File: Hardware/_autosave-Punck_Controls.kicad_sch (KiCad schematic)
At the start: 36 parts, among them J1 Conn_01x12_Female, J10 Kick_In, J11 USB_B_Micro, J12 Tempo_Out, J13 Audio_Out_L, J14 Audio_Out_R, J15 Midi_In, J2 Conn_01x12_Female, J3 Conn_01x12_Female, J4 Conn_01x12_Female, J5 Snare_In, J6 CH_In, J7 OH_In, J8 SamplerA_In, J9 SamplerB_In

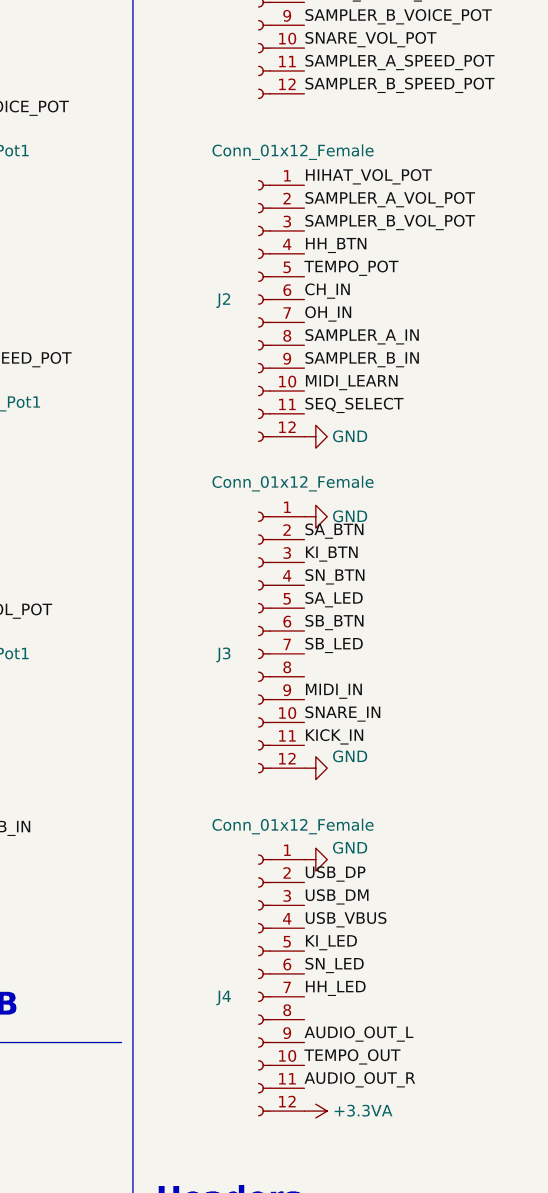
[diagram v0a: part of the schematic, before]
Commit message: Updated PCBs to match changes in panel; ground returns improved
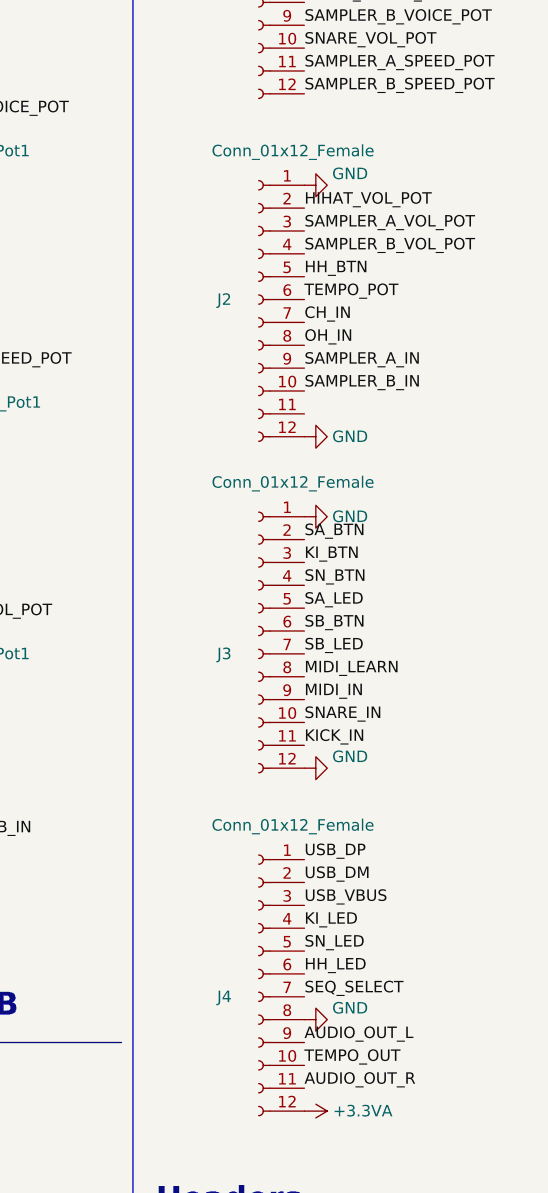
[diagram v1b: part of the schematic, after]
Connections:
- net CH_IN: now also J2.7 (Pin_7); no longer J2.6 (Pin_6)
- net GND: now also J2.1 (Pin_1), J4.8 (Pin_8); no longer J4.1 (Pin_1)
- net HH_BTN: now also J2.5 (Pin_5); no longer J2.4 (Pin_4)
- net HH_LED: now also J4.6 (Pin_6); no longer J4.7 (Pin_7)
- net HIHAT_VOL_POT: now also J2.2 (Pin_2); no longer J2.1 (Pin_1)
- net KI_LED: now also J4.4 (Pin_4); no longer J4.5 (Pin_5)
- net MIDI_LEARN: now also J3.8 (Pin_8); no longer J2.10 (Pin_10)
- net OH_IN: now also J2.8 (Pin_8); no longer J2.7 (Pin_7)
- net SAMPLER_A_IN: now also J2.9 (Pin_9); no longer J2.8 (Pin_8)
- net SAMPLER_A_VOL_POT: now also J2.3 (Pin_3); no longer J2.2 (Pin_2)
- net SAMPLER_B_IN: now also J2.10 (Pin_10); no longer J2.9 (Pin_9)
- net SAMPLER_B_VOL_POT: now also J2.4 (Pin_4); no longer J2.3 (Pin_3)
- net SEQ_SELECT: now also J4.7 (Pin_7); no longer J2.11 (Pin_11)
- net SN_LED: now also J4.5 (Pin_5); no longer J4.6 (Pin_6)
- net TEMPO_POT: now also J2.6 (Pin_6); no longer J2.5 (Pin_5)
- net USB_DM: now also J4.2 (Pin_2); no longer J4.3 (Pin_3)
- net USB_DP: now also J4.1 (Pin_1); no longer J4.2 (Pin_2)
- net USB_VBUS: now also J4.3 (Pin_3); no longer J4.4 (Pin_4)
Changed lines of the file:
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@@
     (effects (font (size 1.27 1.27)) (justify left bottom))
   )
-  (label "CH_IN" (at 252.73 71.12 0)
+  (label "CH_IN" (at 252.73 73.66 0)
     (effects (font (size 1.27 1.27)) (justify left bottom))
   )
@@
     (effects (font (size 1.27 1.27)) (justify left bottom))
   )
-  (label "KI_LED" (at 252.73 143.51 0)
-    (effects (font (size 1.27 1.27)) (justify left bottom))
-  )
-  (label "SAMPLER_A_VOL_POT" (at 252.73 60.96 0)
+  (label "KI_LED" (at 252.73 140.97 0)
+    (effects (font (size 1.27 1.27)) (justify left bottom))
+  )
+  (label "SAMPLER_A_VOL_POT" (at 252.73 63.5 0)
     (effects (font (size 1.27 1.27)) (justify left bottom))
   )
@@
     (effects (font (size 1.27 1.27)) (justify left bottom))
   )
-  (label "USB_DM" (at 252.73 138.43 0)
+  (label "USB_DM" (at 252.73 135.89 0)
     (effects (font (size 1.27 1.27)) (justify left bottom))
   )
@@
     (effects (font (size 1.27 1.27)) (justify left bottom))
   )
-  (label "USB_VBUS" (at 252.73 140.97 0)
+  (label "USB_VBUS" (at 252.73 138.43 0)
     (effects (font (size 1.27 1.27)) (justify left bottom))
   )
@@
     (effects (font (size 1.27 1.27)) (justify left bottom))
   )
-  (label "SEQ_SELECT" (at 252.73 83.82 0)
+  (label "SEQ_SELECT" (at 252.73 148.59 0)
     (effects (font (size 1.27 1.27)) (justify left bottom))
   )
@@
     (effects (font (size 1.27 1.27)) (justify left bottom))
   )
-  (label "HH_BTN" (at 252.73 66.04 0)
-    (effects (font (size 1.27 1.27)) (justify left bottom))
-  )
-  (label "HIHAT_VOL_POT" (at 252.73 58.42 0)
-    (effects (font (size 1.27 1.27)) (justify left bottom))
-  )
-  (label "SN_LED" (at 252.73 146.05 0)
-    (effects (font (size 1.27 1.27)) (justify left bottom))
-  )
-  (label "HH_LED" (at 252.73 148.59 0)
-    (effects (font (size 1.27 1.27)) (justify left bottom))
-  )
-  (label "USB_DP" (at 252.73 135.89 0)
+  (label "HH_BTN" (at 252.73 68.58 0)
+    (effects (font (size 1.27 1.27)) (justify left bottom))
+  )
+  (label "HIHAT_VOL_POT" (at 252.73 60.96 0)
+    (effects (font (size 1.27 1.27)) (justify left bottom))
+  )
+  (label "SN_LED" (at 252.73 143.51 0)
+    (effects (font (size 1.27 1.27)) (justify left bottom))
+  )
+  (label "HH_LED" (at 252.73 146.05 0)
+    (effects (font (size 1.27 1.27)) (justify left bottom))
+  )
+  (label "USB_DP" (at 252.73 133.35 0)
     (effects (font (size 1.27 1.27)) (justify left bottom))
   )
@@
     (effects (font (size 1.27 1.27)) (justify right bottom))
   )
-  (label "MIDI_LEARN" (at 252.73 81.28 0)
+  (label "MIDI_LEARN" (at 252.73 113.03 0)
     (effects (font (size 1.27 1.27)) (justify left bottom))
   )
@@
     (effects (font (size 1.27 1.27)) (justify right bottom))
   )
-  (label "SAMPLER_A_IN" (at 252.73 76.2 0)
+  (label "SAMPLER_A_IN" (at 252.73 78.74 0)
     (effects (font (size 1.27 1.27)) (justify left bottom))
   )
@@
     (effects (font (size 1.27 1.27)) (justify left bottom))
   )
-  (label "SAMPLER_B_IN" (at 252.73 78.74 0)
+  (label "SAMPLER_B_IN" (at 252.73 81.28 0)
     (effects (font (size 1.27 1.27)) (justify left bottom))
   )
@@
     (effects (font (size 1.27 1.27)) (justify left bottom))
   )
-  (label "OH_IN" (at 252.73 73.66 0)
+  (label "OH_IN" (at 252.73 76.2 0)
     (effects (font (size 1.27 1.27)) (justify left bottom))
   )
@@
     (effects (font (size 1.27 1.27)) (justify left bottom))
   )
-  (label "SAMPLER_B_VOL_POT" (at 252.73 63.5 0)
+  (label "SAMPLER_B_VOL_POT" (at 252.73 66.04 0)
     (effects (font (size 1.27 1.27)) (justify left bottom))
   )
@@
     (effects (font (size 1.27 1.27)) (justify left bottom))
   )
-  (label "TEMPO_POT" (at 252.73 68.58 0)
+  (label "TEMPO_POT" (at 252.73 71.12 0)
     (effects (font (size 1.27 1.27)) (justify left bottom))
   )
@@
     (pin "1")
   )
-  (symbol (lib_id "power:GND") (at 252.73 133.35 90) (unit 1)
-    (in_bom yes) (on_board yes)
-    (property "Reference" "#PWR0101" (id 0) (at 259.08 133.35 0)
-      (effects (font (size 1.27 1.27)) hide)
-    )
-    (property "Value" "GND" (id 1) (at 257.81 132.08 90))
-    (property "Footprint" "" (id 2) (at 252.73 133.35 0)
-      (effects (font (size 1.27 1.27)) hide)
-    )
-    (property "Datasheet" "" (id 3) (at 252.73 133.35 0)
+  (symbol (lib_id "power:GND") (at 252.73 151.13 90) (unit 1)
+    (in_bom yes) (on_board yes)
+    (property "Reference" "#PWR0101" (id 0) (at 259.08 151.13 0)
+      (effects (font (size 1.27 1.27)) hide)
+    )
+    (property "Value" "GND" (id 1) (at 257.81 149.86 90))
+    (property "Footprint" "" (id 2) (at 252.73 151.13 0)
+      (effects (font (size 1.27 1.27)) hide)
+    )
+    (property "Datasheet" "" (id 3) (at 252.73 151.13 0)
       (effects (font (size 1.27 1.27)) hide)
     )
@@
     (pin "3")
   )
+  (symbol (lib_id "power:GND") (at 252.73 58.42 90) (unit 1)
+    (in_bom yes) (on_board yes)
+    (property "Reference" "#PWR0107" (id 0) (at 259.08 58.42 0)
+      (effects (font (size 1.27 1.27)) hide)
+    )
+    (property "Value" "GND" (id 1) (at 257.81 57.15 90))
+    (property "Footprint" "" (id 2) (at 252.73 58.42 0)
+      (effects (font (size 1.27 1.27)) hide)
+    )
+    (property "Datasheet" "" (id 3) (at 252.73 58.42 0)
+      (effects (font (size 1.27 1.27)) hide)
+    )
+    (pin "1")
+  )
   (symbol (lib_id "power:GND") (at 252.73 20.32 90) (unit 1)
     (in_bom yes) (on_board yes)
@@
       (reference "#PWR0106") (unit 1) (value "+3.3VA") (footprint "")
     )
+    (path "/c269bd85-a27f-4da9-a399-1bdfcd17cddb"
+      (reference "#PWR0107") (unit 1) (value "GND") (footprint "")
+    )
     (path "/990184b4-4444-4c3c-9341-d5ee4a989dd2"
